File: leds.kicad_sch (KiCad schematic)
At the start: 66 parts

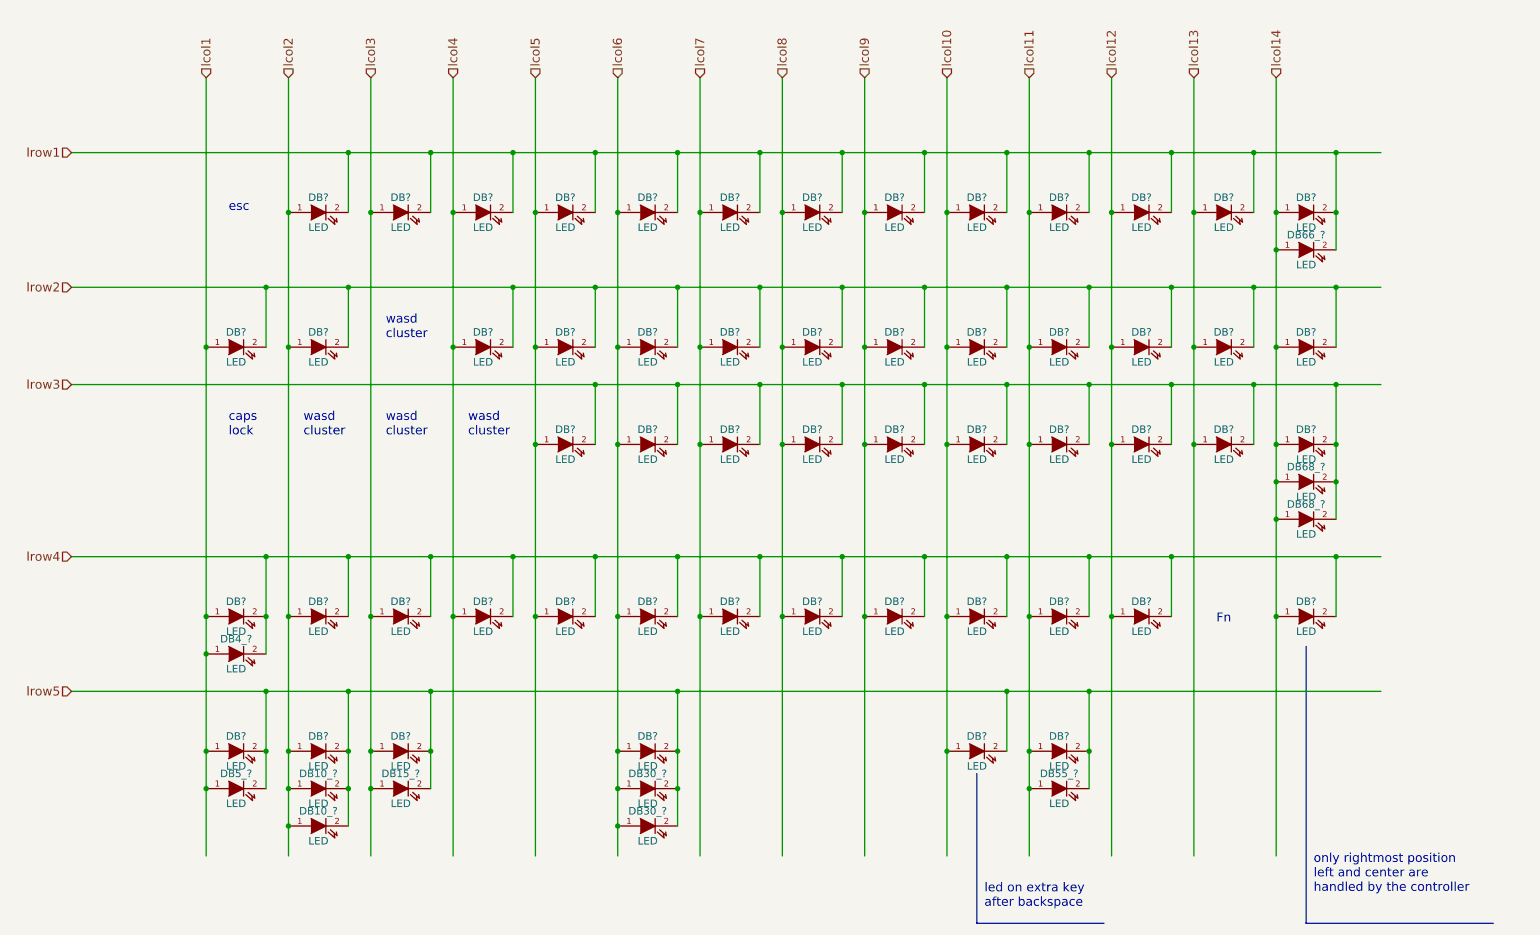
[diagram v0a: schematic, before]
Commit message: add gh60 lib to project
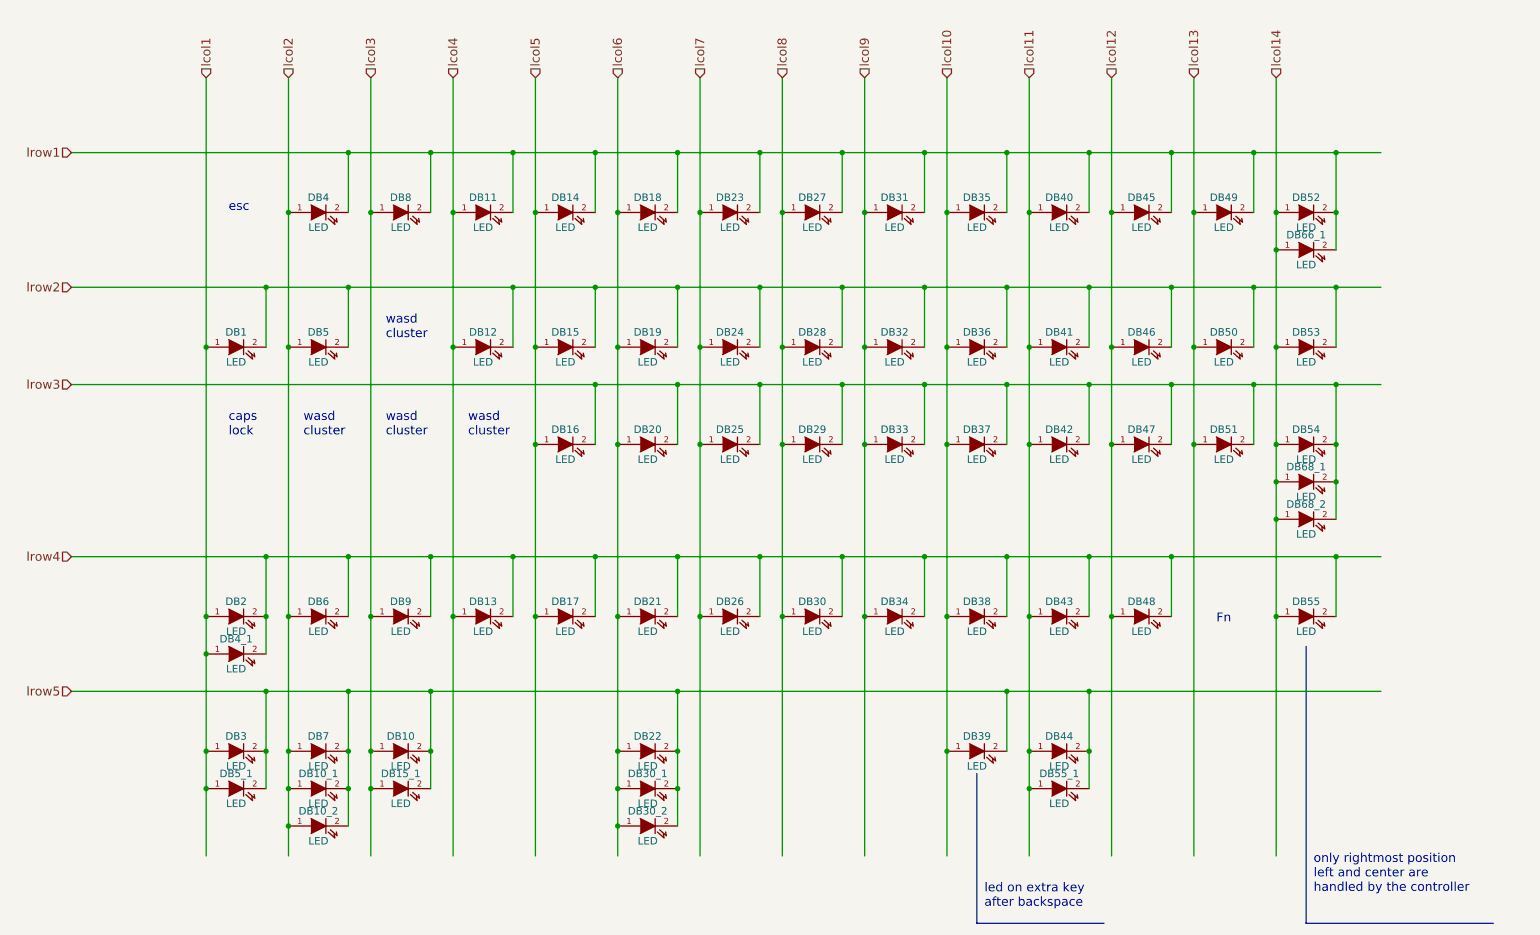
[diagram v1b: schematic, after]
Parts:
- gave numbers to parts that had none: 66
